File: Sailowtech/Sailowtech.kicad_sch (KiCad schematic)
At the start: 12 parts, among them J1 Second Board Connector, U1 Zigbee, U2 ESP32-DEVKITM-1

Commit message: SecondBoard Rond m130
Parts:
- removed I2C_3.3V_GND_SDA_SCL1, I2C_3.3V_GND_SDA_SCL2: ~, TerminalBlock_Phoenix:TerminalBlock_Phoenix_MKDS-1,5-4_1x04_P5.00mm_Horizontal, symbol Connector:Conn_01x04_Socket
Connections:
- net SCL: no longer names the net of J1.8, U2.J3_5 (GPIO22)
- net SCL: no longer U2.J1_11 (GPIO33)
- net SDA: no longer names the net of J1.10, U2.J3_4 (GPIO21)
- net SDA: no longer U2.J1_10 (GPIO32)

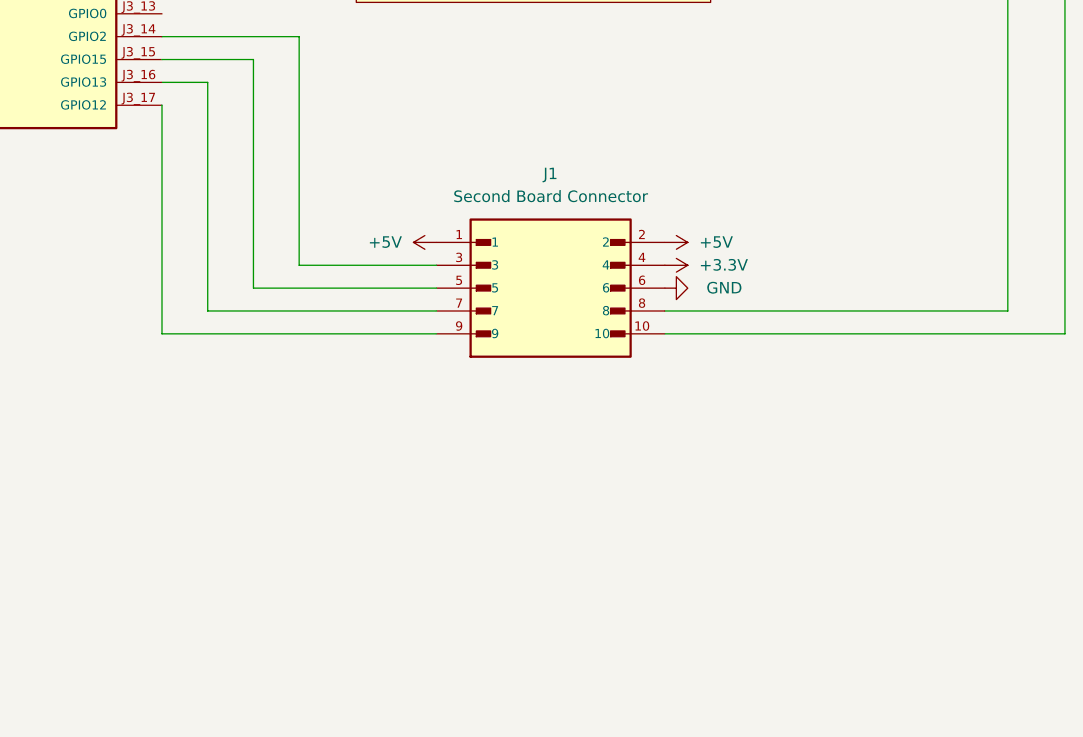
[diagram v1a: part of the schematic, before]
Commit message: changement connecteur
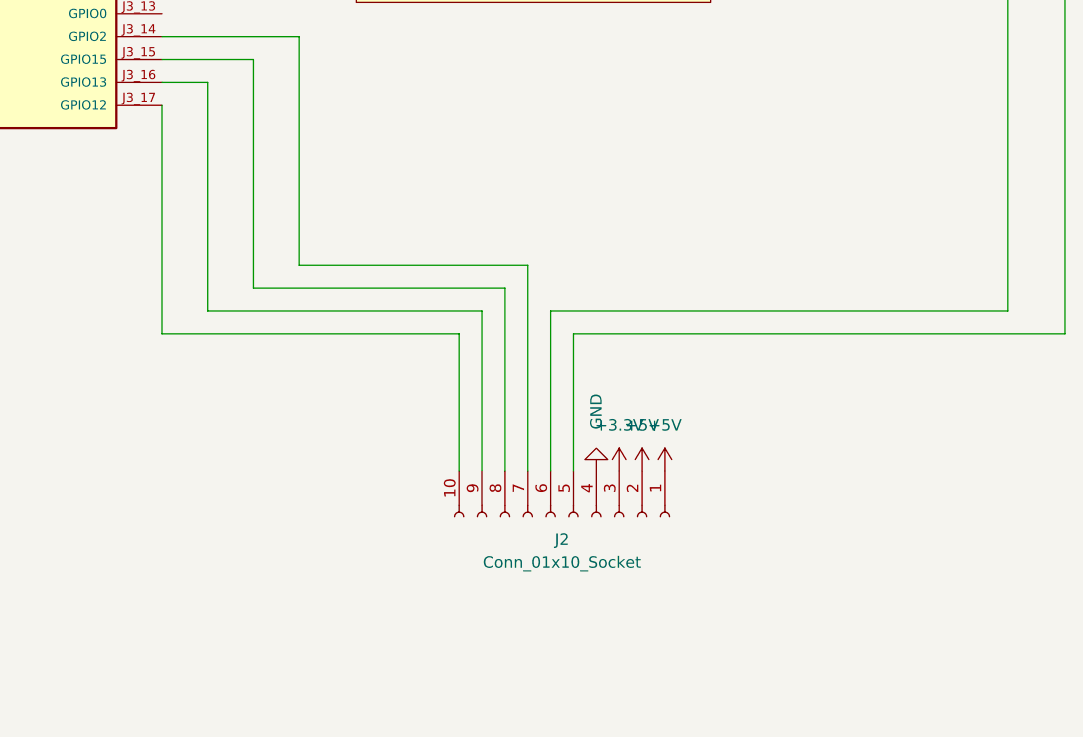
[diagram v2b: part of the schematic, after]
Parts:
- removed J1: Second Board Connector, M50-3550542:HARWIN_M50-3550542, symbol M50-3550542:M50-3550542
- added J2: Conn_01x10_Socket, Connector_PinHeader_2.54mm:PinHeader_1x10_P2.54mm_Vertical, symbol Connector:Conn_01x10_Socket
- Battery1: footprint TerminalBlock_Phoenix:TerminalBlock_Phoenix_MKDS-1,5-2_1x02_P5.00mm_Horizontal -> Connector_Phoenix_MC:PhoenixContact_MCV_1,5_2-G-3.5_1x02_P3.50mm_Vertical
- NMEA1: footprint TerminalBlock_Phoenix:TerminalBlock_Phoenix_MKDS-1,5-4_1x04_P5.00mm_Horizontal -> Connector_Phoenix_MC:PhoenixContact_MCV_1,5_4-G-3.5_1x04_P3.50mm_Vertical
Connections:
- net +3.3V: now also J2.3 (Pin_3)
- net +5V: now also J2.1 (Pin_1), J2.2 (Pin_2)
- net GND: now also J2.4 (Pin_4)
- net at U2.J3_14 (GPIO2): now also J2.7 (Pin_7)
- net at U2.J3_15 (GPIO15): now also J2.8 (Pin_8)
- net at U2.J3_16 (GPIO13): now also J2.9 (Pin_9)
- net at U2.J3_17 (GPIO12): now also J2.10 (Pin_10)
- net at U2.J3_4 (GPIO21): now also J2.5 (Pin_5)
- net at U2.J3_5 (GPIO22): now also J2.6 (Pin_6)
